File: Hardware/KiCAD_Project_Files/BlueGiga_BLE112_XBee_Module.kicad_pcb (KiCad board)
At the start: 4 copper layers, 24.5 x 24.4 mm, 9 parts, among them P1 XBEE HEADER, P2 DEBUG, U1 BLE112-A

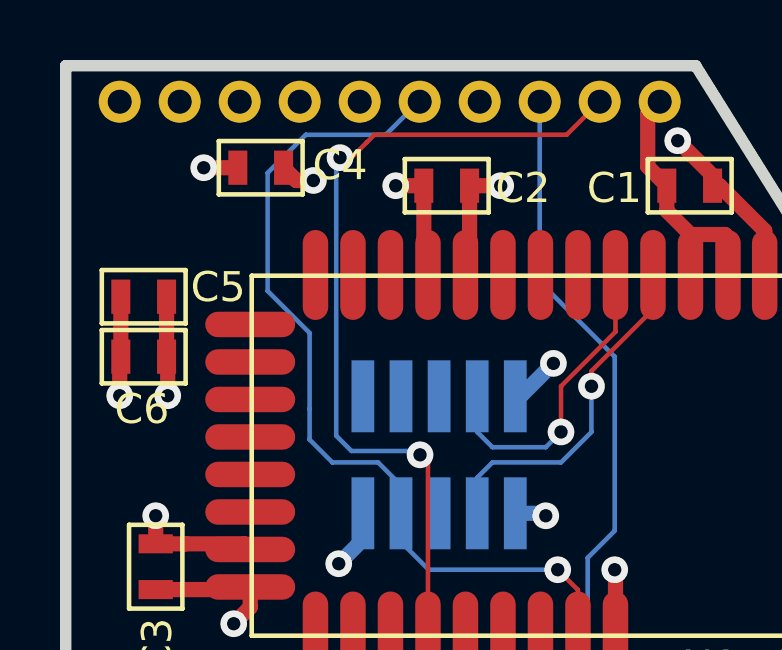
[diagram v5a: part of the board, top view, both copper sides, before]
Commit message: Fixed layout/gerber issue shorting the power and ground plane together through two vias that did not have their clearance refreshed after the copper pour was filled.
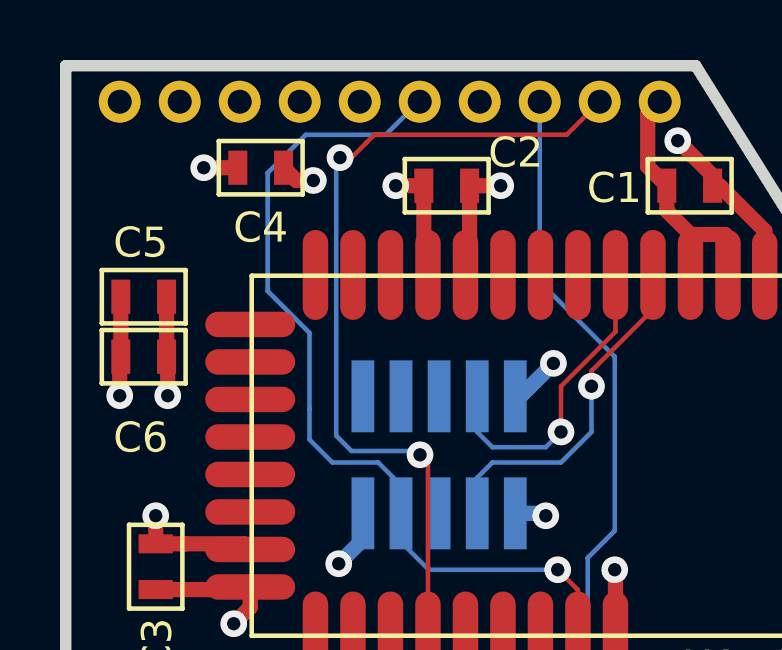
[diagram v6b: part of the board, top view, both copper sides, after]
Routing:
- added copper zone on Pwr.Cu, net +3V3
- added copper zone on Gnd.Cu, net GND
- removed copper zone on Inner2-Pwr.Cu, net +3V3
- removed copper zone on Inner3-Gnd.Cu, net GND
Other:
- board text added: "REV 5"
- board text removed: "REV 4"
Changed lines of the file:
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@@
-(kicad_pcb (version 4) (host pcbnew "(after 2015-mar-04 BZR unknown)-product")
+(kicad_pcb (version 4) (host pcbnew "(2015-07-11 BZR 5925, Git c291b88)-product")
   (general
     (links 31)
@@
   (page USLetter)
   (title_block
-    (date "Saturday, May 02, 2015")
-    (rev 4.0)
+    (date 2015-07-15)
+    (rev 5.0)
   )
   (layers
     (0 Front signal)
-    (1 Inner2-Pwr.Cu signal)
-    (2 Inner3-Gnd.Cu signal)
+    (1 Pwr.Cu signal hide)
+    (2 Gnd.Cu signal hide)
     (31 Back signal)
     (32 B.Adhes user)
@@
     (visible_elements 7FFEFFFF)
     (pcbplotparams
-      (layerselection 0x010fc_80000007)
-      (usegerberextensions true)
+      (layerselection 0x011fc_80000007)
+      (usegerberextensions false)
       (excludeedgelayer true)
       (linewidth 0.150000)
@@
       (drillshape 0)
       (scaleselection 1)
-      (outputdirectory P:/Engineering_SECURE/Projects/BlueGiga_BLE112_XBee_Module/Hardware/Gerbers/))
+      (outputdirectory P:/Engineering_SECURE/Projects/Bluetooth_LE/BlueGiga_BLE112_XBee_Module/Hardware/Gerbers/))
   )
   (net 0 "")
@@
     (at 111.446 93.57 180)
     (tags Header)
-    (fp_text reference P2 (at -4.454 1.27 450) (layer B.SilkS)
+    (fp_text reference P2 (at -5.054 -0.93 450) (layer B.SilkS)
       (effects (font (size 1 1) (thickness 0.1524)) (justify mirror))
     )
@@
     (at 101.6 90.3 180)
     (attr smd)
-    (fp_text reference C6 (at 0.06 -1.746 180) (layer F.SilkS)
+    (fp_text reference C6 (at 0.1 -2.7 180) (layer F.SilkS)
       (effects (font (size 1 1) (thickness 0.1524)))
     )
@@
     (at 101.6 88.3 180)
     (attr smd)
-    (fp_text reference C5 (at -2.48 0.318 180) (layer F.SilkS)
+    (fp_text reference C5 (at 0.1 1.8 180) (layer F.SilkS)
       (effects (font (size 1 1) (thickness 0.1524)))
     )
@@
     (at 105.5 84)
     (attr smd)
-    (fp_text reference C4 (at 2.644 -0.082) (layer F.SilkS)
+    (fp_text reference C4 (at 0 2) (layer F.SilkS)
       (effects (font (size 1 1) (thickness 0.1524)))
     )
@@
     (at 111.7 84.6 180)
     (attr smd)
-    (fp_text reference C2 (at -2.54 -0.08 180) (layer F.SilkS)
+    (fp_text reference C2 (at -2.3 1.1 180) (layer F.SilkS)
       (effects (font (size 1 1) (thickness 0.1524)))
     )
@@
   )
   (gr_circle (center 115.5 96.5) (end 116 96.5) (layer B.SilkS) (width 0.254))
-  (gr_text "REV 4" (at 118 90 270) (layer B.SilkS)
+  (gr_text "REV 5" (at 118 90 270) (layer B.SilkS)
     (effects (font (size 1.016 1.016) (thickness 0.1524)) (justify mirror))
   )
@@
   (segment (start 108.906 96.394) (end 108.1 97.2) (width 0.508) (layer Back) (net 9))
   (segment (start 108.906 95.52) (end 108.906 96.394) (width 0.508) (layer Back) (net 9))
-  (zone (net 2) (net_name GND) (layer Inner3-Gnd.Cu) (hatch edge 0.508)
+  (zone (net 2) (net_name GND) (layer Gnd.Cu) (hatch edge 0.508)
     (connect_pads (clearance 0.254))
     (min_thickness 0.254)
@@
     )
   )
-  (zone (net 9) (net_name +3V3) (layer Inner2-Pwr.Cu) (hatch edge 0.508)
+  (zone (net 9) (net_name +3V3) (layer Pwr.Cu) (hatch edge 0.508)
     (connect_pads (clearance 0.254))
     (min_thickness 0.254)

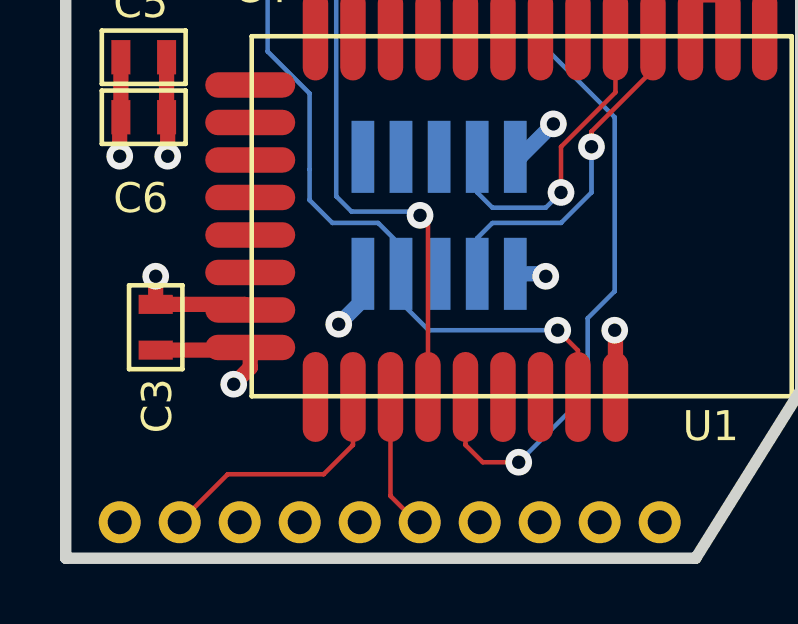
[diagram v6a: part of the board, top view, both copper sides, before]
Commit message: Corrected debug header connections where pin 9 was connected to 3.3V.
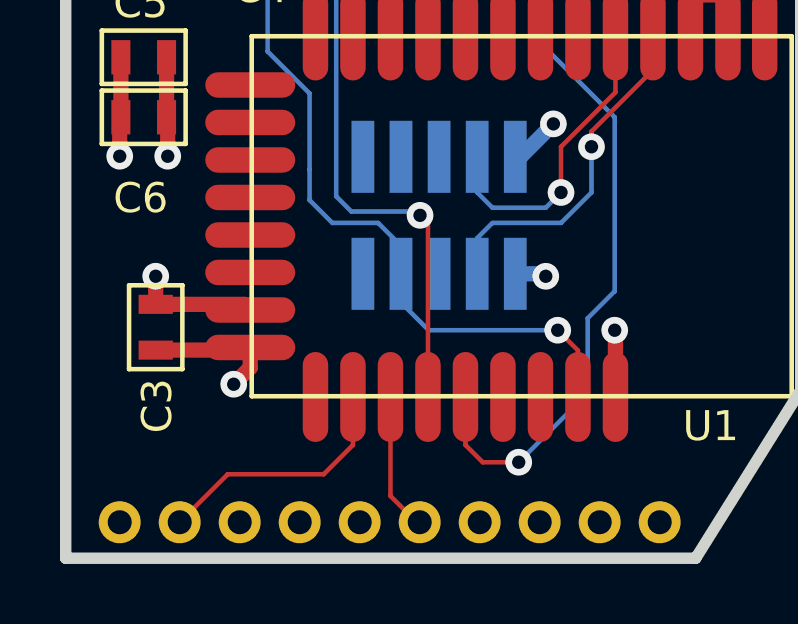
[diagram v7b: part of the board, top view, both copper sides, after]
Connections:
- P2 pad 9: +3V3 -> Net-(P2-Pad9)
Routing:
- net +3V3: track 28.3 -> 26.2 mm, vias 6 -> 5
- net Net-(P2-Pad9): track 0.00 -> 0.96 mm
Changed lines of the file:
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@@
 (kicad_pcb (version 4) (host pcbnew "(2015-07-11 BZR 5925, Git c291b88)-product")
   (general
-    (links 31)
+    (links 30)
     (no_connects 0)
-    (area 98.809499 80.409499 123.690501 105.190501)
+    (area 85.517999 72.8948 129.691934 105.190501)
     (thickness 1.6002)
     (drawings 12)
-    (tracks 129)
+    (tracks 127)
     (zones 0)
     (modules 9)
-    (nets 42)
+    (nets 43)
   )
   (page USLetter)
@@
   (layers
     (0 Front signal)
-    (1 Pwr.Cu signal hide)
-    (2 Gnd.Cu signal hide)
+    (1 Pwr.Cu signal)
+    (2 Gnd.Cu signal)
     (31 Back signal)
     (32 B.Adhes user)
@@
       (layerselection 0x011fc_80000007)
       (usegerberextensions false)
-      (excludeedgelayer true)
+      (excludeedgelayer false)
       (linewidth 0.150000)
-      (plotframeref false)
+      (plotframeref true)
       (viasonmask false)
       (mode 1)
-      (useauxorigin true)
+      (useauxorigin false)
       (hpglpennumber 1)
       (hpglpenspeed 20)
@@
       (padsonsilk false)
       (subtractmaskfromsilk false)
-      (outputformat 1)
+      (outputformat 4)
       (mirror false)
       (drillshape 0)
       (scaleselection 1)
-      (outputdirectory P:/Engineering_SECURE/Projects/Bluetooth_LE/BlueGiga_BLE112_XBee_Module/Hardware/Gerbers/))
+      (outputdirectory P:/Engineering_SECURE/Projects/Bluetooth_LE/BlueGiga_BLE112_XBee_Module/Hardware/Drawing/))
   )
   (net 0 "")
@@
   (net 40 "Net-(P2-Pad8)")
   (net 41 "Net-(P2-Pad10)")
+  (net 42 "Net-(P2-Pad9)")
   (net_class Default "This is the default net class."
     (clearance 0.1524)
@@
     (add_net "Net-(P2-Pad6)")
     (add_net "Net-(P2-Pad8)")
+    (add_net "Net-(P2-Pad9)")
     (add_net "Net-(U1-Pad11)")
     (add_net "Net-(U1-Pad12)")
@@
       (net 40 "Net-(P2-Pad8)"))
     (pad 9 smd rect (at 2.54 -1.95 180) (size 0.76 2.4) (layers Back B.Paste B.Mask)
-      (net 9 +3V3))
+      (net 42 "Net-(P2-Pad9)"))
     (pad 10 smd rect (at 2.54 1.95 180) (size 0.76 2.4) (layers Back B.Paste B.Mask)
       (net 41 "Net-(P2-Pad10)"))
@@
   (segment (start 119.038 85.438) (end 119.825 86.225) (width 0.508) (layer Front) (net 9))
   (segment (start 119.038 84.6) (end 119.038 85.438) (width 0.508) (layer Front) (net 9))
-  (segment (start 108.906 95.52) (end 108.906 95.602) (width 0.508) (layer Back) (net 9))
   (segment (start 114.158 91.62) (end 115.256 90.522) (width 0.508) (layer Back) (net 9))
   (via (at 115.256 90.522) (size 0.889) (layers Front Back) (net 9))
@@
   (via (at 102 95.6) (size 0.889) (layers Front Back) (net 9))
   (segment (start 102 96.538) (end 102 95.6) (width 0.508) (layer Front) (net 9))
-  (via (at 108.1 97.2) (size 0.889) (layers Front Back) (net 9))
-  (segment (start 108.906 96.394) (end 108.1 97.2) (width 0.508) (layer Back) (net 9))
-  (segment (start 108.906 95.52) (end 108.906 96.394) (width 0.508) (layer Back) (net 9))
+  (segment (start 108.906 95.52) (end 108.906 95.602) (width 0.508) (layer Back) (net 42))
+  (segment (start 108.906 95.52) (end 108.906 96.394) (width 0.508) (layer Back) (net 42))
   (zone (net 2) (net_name GND) (layer Gnd.Cu) (hatch edge 0.508)
     (connect_pads (clearance 0.254))
